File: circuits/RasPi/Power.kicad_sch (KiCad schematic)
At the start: 102 parts, among them J4 Conn_01x02_Pin, Q11 2N7002, Q12 SSM6J808R, Q14 SSM6J808R, Q15 S8550, Q16 SSM6J808R, Q17 S8550, Q31 MTP4835I3, Q6 SSM3J332R, Q7 S8550, Q8 SSM3J332R, Q9 S8550, SW4 SW_SPDT, U13 TPS54560BDDA, U16 AZ1117CH-3.3, U17 M51957B, U19 DCDC_TPS61023, U21 74AHC1G02, U22 NJM2732

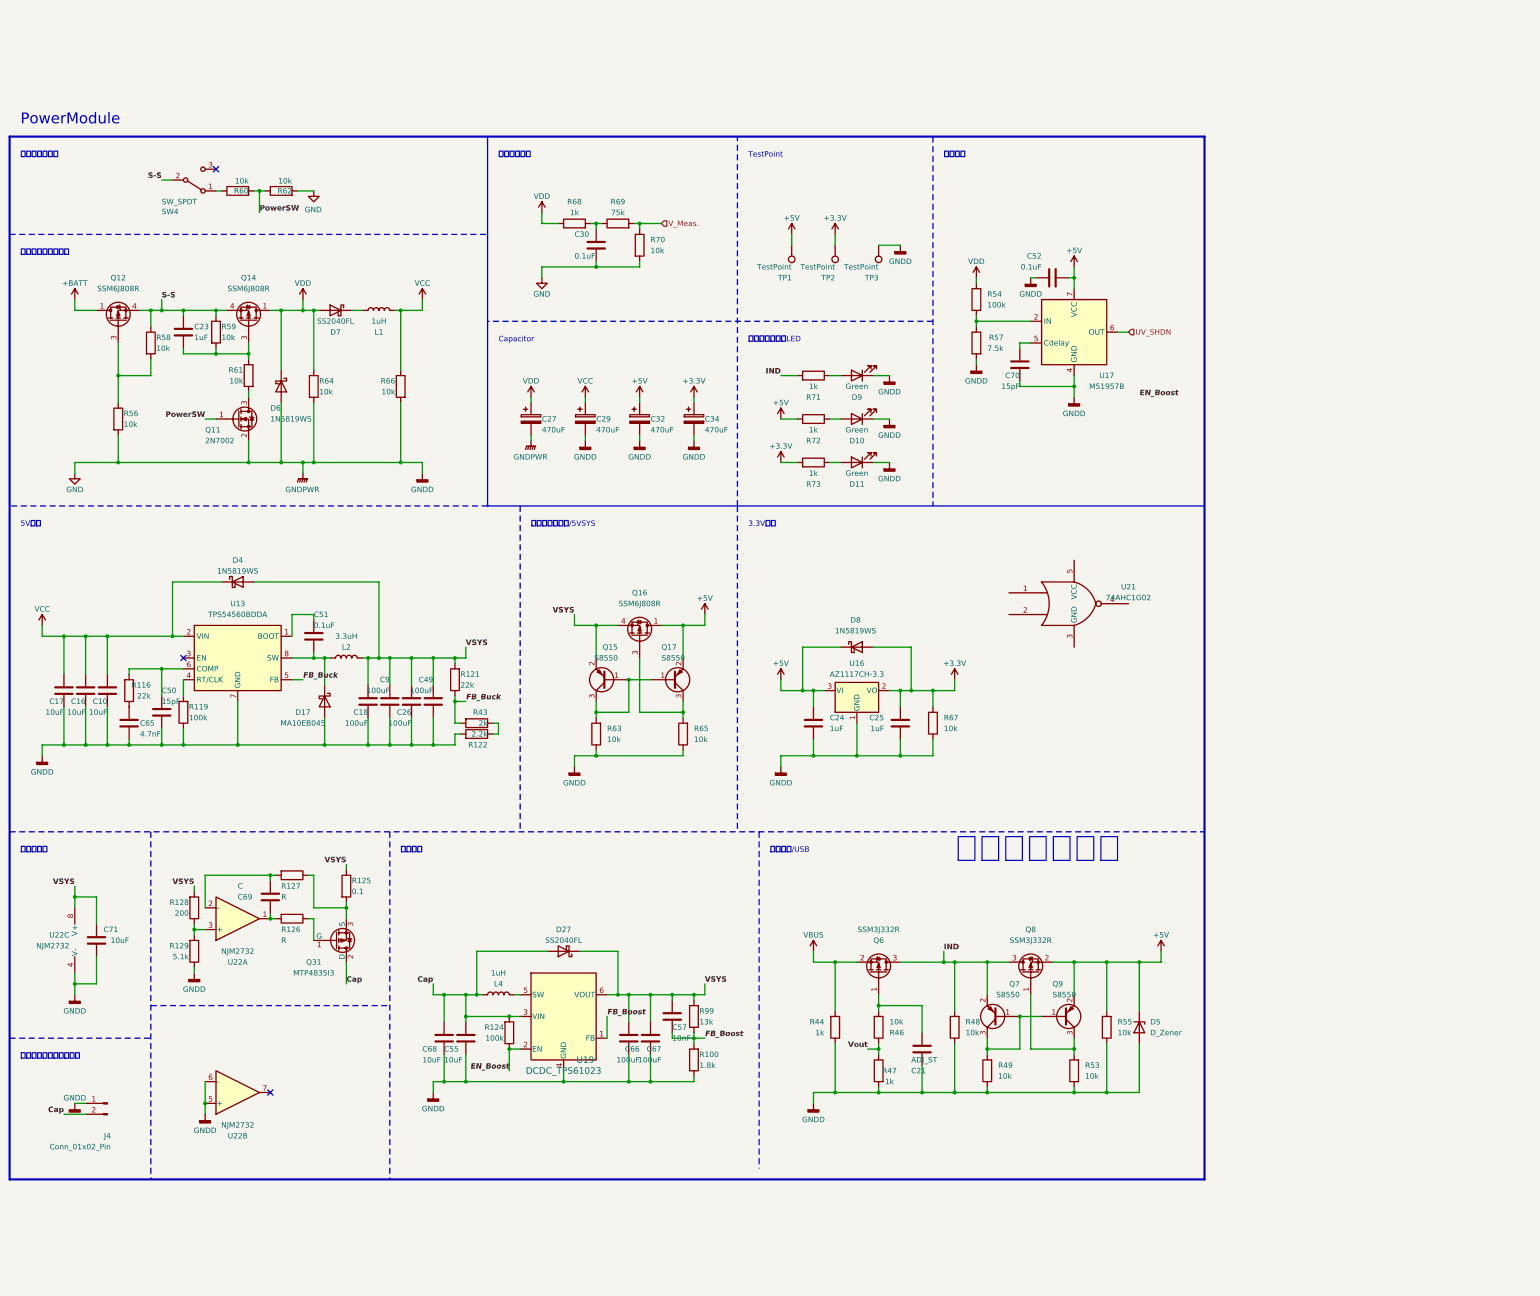
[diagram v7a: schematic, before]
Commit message: 発注_第一弾
Drive, 1stLayer_Power, 2ndLayer_3rdLayer
を発注
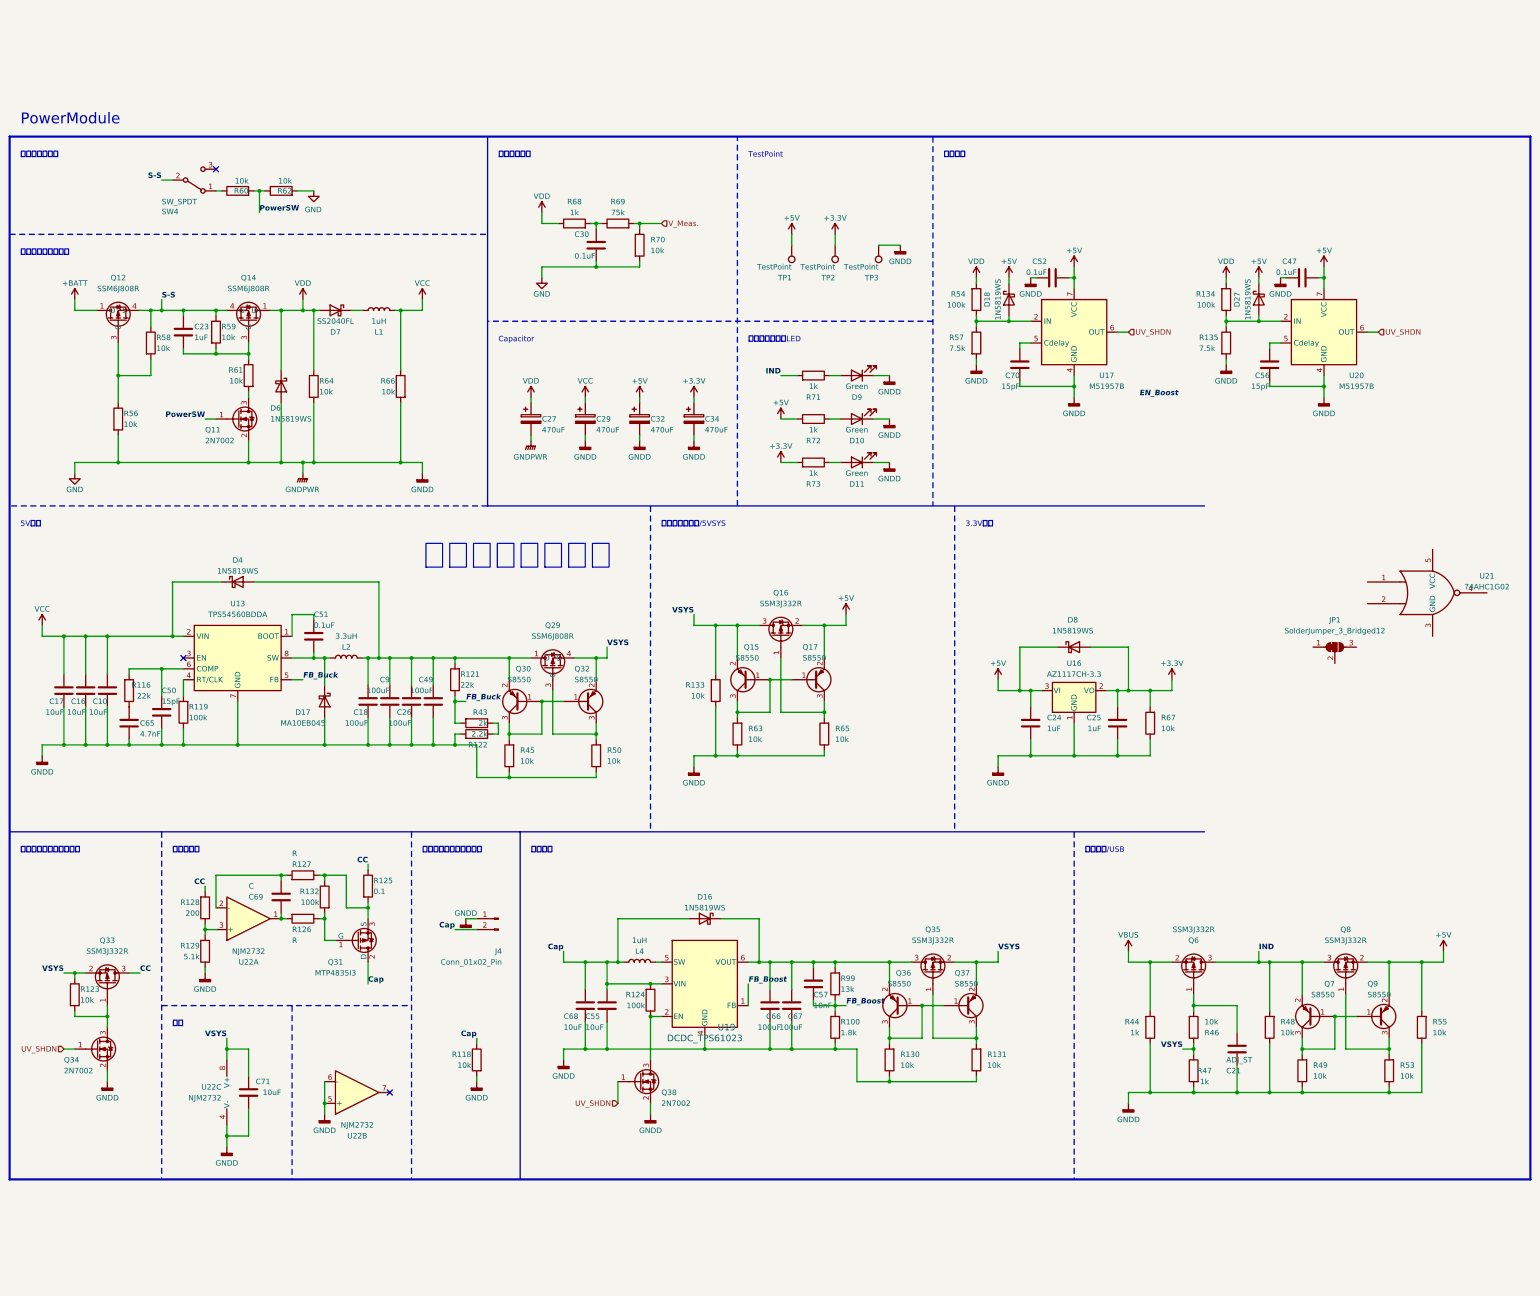
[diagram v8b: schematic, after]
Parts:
- removed D5: D_Zener, Diode_SMD:D_SOD-323_HandSoldering, symbol Device:D_Zener
- removed Q16: SSM6J808R, Package_SO:TSOP-6_1.65x3.05mm_P0.95mm, symbol Transistor_FET:PMN48XP
- added C47: 0.1uF, Capacitor_SMD:C_0402_1005Metric, symbol Device:C
- added C56: 15pF, Capacitor_SMD:C_0402_1005Metric, symbol Device:C
- added D16, D18: 1N5819WS, Diode_SMD:D_SOD-323_HandSoldering, symbol Device:D_Schottky
- added JP1: SolderJumper_3_Bridged12, Jumper:SolderJumper-3_P1.3mm_Bridged12_RoundedPad1.0x1.5mm, symbol Jumper:SolderJumper_3_Bridged12
- added Q16, Q33, Q35: SSM3J332R, Package_TO_SOT_SMD:SOT-23W, symbol Device:Q_PMOS_GSD
- added Q29: SSM6J808R, TomoshibiLibrary:Package_TSOP6F, symbol Transistor_FET:PMN48XP
- added Q30, Q32, Q36, Q37: S8550, Package_TO_SOT_SMD:SOT-23, symbol Device:Q_PNP_BEC
- added Q34, Q38: 2N7002, Package_TO_SOT_SMD:SOT-23, symbol Transistor_FET:2N7002
- added R118, R123, R130, R131, R133, R45, R50: 10k, Resistor_SMD:R_0402_1005Metric, symbol Device:R
- added R132: 100k, Resistor_SMD:R_0402_1005Metric, symbol Device:R
- added R134: 100k, Resistor_SMD:R_0603_1608Metric, symbol Device:R
- added R135: 7.5k, Resistor_SMD:R_0603_1608Metric, symbol Device:R
- added U20: M51957B, Package_SO:SOP-8_3.9x4.9mm_P1.27mm, symbol TomoshibiLibrary:Power_Supervisor_M51957B
- D27: value SS2040FL -> 1N5819WS; footprint Diode_SMD:D_SOD-123 -> Diode_SMD:D_SOD-323_HandSoldering
- Q12, Q14: footprint Package_SO:TSOP-6_1.65x3.05mm_P0.95mm -> TomoshibiLibrary:Package_TSOP6F
- R125: footprint (none) -> Resistor_SMD:R_1210_3225Metric
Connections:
- net Vout is gone; now on net VSYS: R46.1, R47.1
- net +5V: now also D27.1 (K), C47.2, D18.1 (K), Q16.2 (S), U20.7 (VCC)
- net Cap: now also D16.2 (A), R118.1; no longer D27.2 (A)
- net EN_Boost: no longer R124.1, U19.2 (EN)
- net GND: now also C47.1, C56.2, Q34.2 (S), Q38.2 (S), R118.2, R130.1, R131.1, R133.1, R135.2, R45.1, R50.1, U20.4 (GND)
- net UV_SHDN: now also Q34.1 (G), Q38.1 (G), U20.6 (OUT)
- net VDD: now also R134.2
- net VSYS: now also Q16.3 (D), Q29.4 (S), Q32.2 (E), Q33.2 (S), Q35.2 (S), Q37.2 (E), R123.1, R133.2; no longer C18.1, C26.1, C49.1, C57.1, C66.1, C67.1, C9.1, D27.1 (K), D4.2 (A), L2.2, R121.2, R125.1, R128.2, R99.2, U19.6 (VOUT)
- net at R54.1, R57.1, U17.2 (IN): now also D18.2 (A)
- net at Q31.1 (G), R126.1: now also R132.2
- net at Q31.3 (S), R125.2, R127.1: now also R132.1
- net at Q17.3 (C), R65.2: now also Q16.1 (G)
- new net: Q33.1 (G), Q34.3 (D), R123.2
- new net: C18.1, C26.1, C49.1, C9.1, D4.2 (A), L2.2, Q29.1 (D), Q29.2 (D), Q29.5 (D), Q29.6 (D), Q30.2 (E), R121.2
- new net: D27.2 (A), R134.1, R135.1, U20.2 (IN)
- new net: C56.1, U20.5 (Cdelay)
- new net: C57.1, C66.1, C67.1, D16.1 (K), Q35.3 (D), Q36.2 (E), R99.2, U19.6 (VOUT)
- new net: Q38.3 (D), R124.1, U19.2 (EN)
- new net: Q36.1 (B), Q36.3 (C), Q37.1 (B), R130.2
- new net: Q35.1 (G), Q37.3 (C), R131.2
- new net: Q30.1 (B), Q30.3 (C), Q32.1 (B), R45.2
- new net: Q29.3 (G), Q32.3 (C), R50.2
- new net CC: Q33.3 (D), R125.1, R128.2
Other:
- note added: "キャパシタ充電スイッチ"
- note added: "ダイオード変更？"
- note added: "電源"
- note removed: "ダイオード変更"
- moved on the sheet: C21, C24, C25, C55, C57, C66, C67, C68, C69, C71, D8, J4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
